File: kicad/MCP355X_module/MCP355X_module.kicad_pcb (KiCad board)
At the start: 2 copper layers, 20.8 x 15.7 mm, 20 parts, among them J1 PINS_1X6, J2 PINS_1X6, U1 MCP355X-E_SN

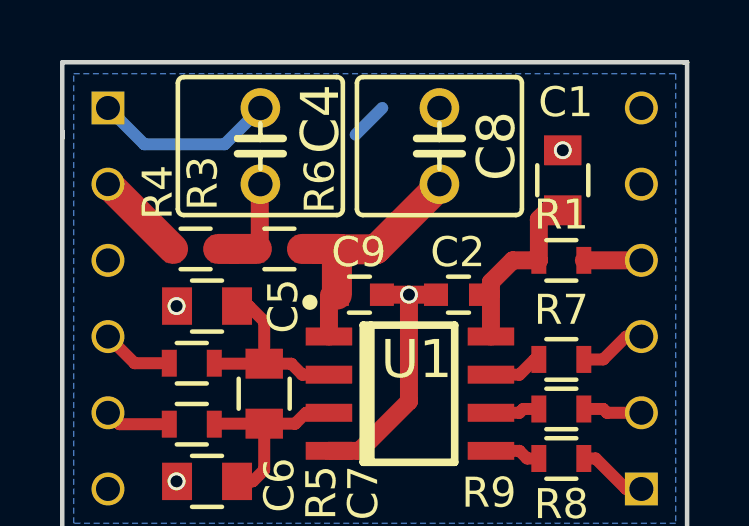
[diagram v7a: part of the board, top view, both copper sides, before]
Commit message: * changes a mistake on layouting on wrong grid
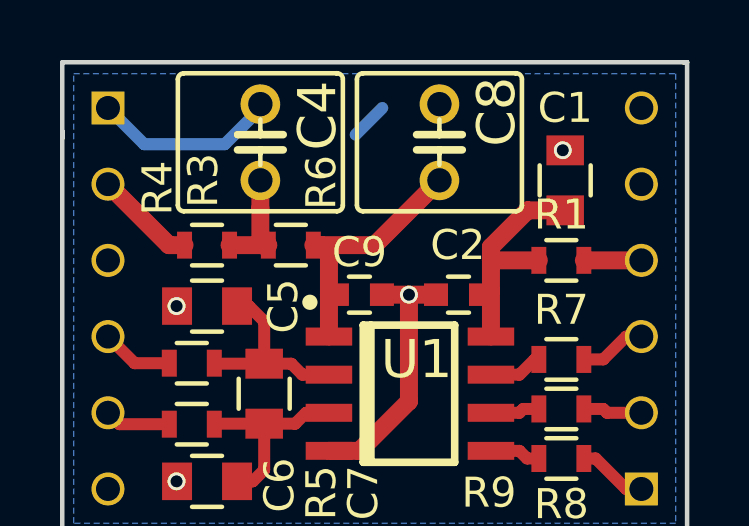
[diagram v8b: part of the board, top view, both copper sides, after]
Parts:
- moved R3 0.40 mm to (145.5, 102.4)
- moved R6 0.40 mm to (148.3, 102.4)
- moved C4 0.13 mm to (147.3, 98.9)
- moved C8 0.13 mm to (153.3, 98.9)
- moved C1 0.08 mm to (157.5, 100.2)
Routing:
- net VDD: track 6.34 -> 7.95 mm
- net GND: track 15.8 -> 14.5 mm
- net (no net): track 0.00 -> 1.26 mm
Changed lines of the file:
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@@
     (links 34)
     (no_connects 6)
-    (area 137.095 91.584714 165.375 115.21)
+    (area 137.095 91.571428 165.375 115.21)
     (thickness 1.6)
     (drawings 7)
-    (tracks 83)
+    (tracks 81)
     (zones 0)
     (modules 20)
@@
   )
   (setup
-    (last_trace_width 1)
+    (last_trace_width 0.6)
     (user_trace_width 0.3)
     (user_trace_width 0.4)
@@
     (tags "resistor 0603")
     (attr smd)
-    (fp_text reference R4 (at 1.134 5.699 450) (layer F.SilkS)
+    (fp_text reference R4 (at 1.143 5.842 450) (layer F.SilkS)
       (effects (font (size 1 1) (thickness 0.15)))
     )
@@
     (tags "capacitor 0603")
     (attr smd)
-    (fp_text reference C2 (at 0.024 1.413 360) (layer F.SilkS)
+    (fp_text reference C2 (at 0.024 1.651 360) (layer F.SilkS)
       (effects (font (size 1 1) (thickness 0.15)))
     )
@@
   )
   (module Resistors_SMD:R_0603 (layer F.Cu)
-    (at 145.161 102.489 180)
+    (at 145.542 102.362 180)
     (descr "Resistor SMD 0603, reflow soldering, Vishay (see dcrcw.pdf)")
     (tags "resistor 0603")
     (attr smd)
-    (fp_text reference R3 (at -0.239 2.189 270) (layer F.SilkS)
+    (fp_text reference R3 (at 0.127 2.159 270) (layer F.SilkS)
       (effects (font (size 1 1) (thickness 0.15)))
     )
@@
   )
   (module Resistors_SMD:R_0603 (layer F.Cu)
-    (at 147.955 102.489 180)
+    (at 148.336 102.362 180)
     (descr "Resistor SMD 0603, reflow soldering, Vishay (see dcrcw.pdf)")
     (tags "resistor 0603")
     (attr smd)
-    (fp_text reference R6 (at -1.345 2.089 270) (layer F.SilkS)
+    (fp_text reference R6 (at -1.016 2.089 270) (layer F.SilkS)
       (effects (font (size 1 1) (thickness 0.15)))
     )
@@
   )
   (module Capacitors_SMD:C_0805 (layer F.Cu)
-    (at 157.4 100.2 90)
+    (at 157.48 100.203 90)
     (descr "Capacitor SMD 0805, reflow soldering, AVX (see smccp.pdf)")
     (tags "capacitor 0805")
     (attr smd)
-    (fp_text reference C1 (at 2.6 0.1 360) (layer F.SilkS)
+    (fp_text reference C1 (at 2.413 0 360) (layer F.SilkS)
       (effects (font (size 1 1) (thickness 0.15)))
     )
@@
     (tags "capacitor 0603")
     (attr smd)
-    (fp_text reference C9 (at 0.022 1.413 180) (layer F.SilkS)
+    (fp_text reference C9 (at 0 1.413 180) (layer F.SilkS)
       (effects (font (size 1 1) (thickness 0.15)))
     )
@@
   )
   (module SquantorRcl:C025-055X046 (layer F.Cu)
-    (at 147.32 99.06 270)
+    (at 147.32 98.933 270)
     (descr CAPACITOR)
     (tags CAPACITOR)
     (attr virtual)
-    (fp_text reference C4 (at -0.9 -2 270) (layer F.SilkS)
+    (fp_text reference C4 (at -0.889 -1.905 270) (layer F.SilkS)
       (effects (font (size 1.27 1.27) (thickness 0.15)))
     )
@@
   )
   (module SquantorRcl:C025-055X046 (layer F.Cu)
-    (at 153.289 99.06 270)
+    (at 153.289 98.933 270)
     (descr CAPACITOR)
     (tags CAPACITOR)
     (attr virtual)
-    (fp_text reference C8 (at 0 -1.9 270) (layer F.SilkS)
+    (fp_text reference C8 (at -1.016 -1.905 270) (layer F.SilkS)
       (effects (font (size 1.27 1.27) (thickness 0.15)))
     )
@@
   (gr_line (start 161.544 112.014) (end 140.716 112.014) (angle 90) (layer Edge.Cuts) (width 0.15))
   (gr_line (start 140.716 96.266) (end 161.544 96.266) (angle 90) (layer Edge.Cuts) (width 0.15))
+  (segment (start 151.384 97.79) (end 150.495 98.679) (width 0.4) (layer B.Cu) (net 0))
   (segment (start 146.13 99) (end 143.45 99) (width 0.4) (layer B.Cu) (net 1))
   (segment (start 143.45 99) (end 142.24 97.79) (width 0.4) (layer B.Cu) (net 1))
@@
   (segment (start 144.526 104.394) (end 144.526 104.394) (width 0.6) (layer B.Cu) (net 1))
   (via (at 144.526 104.394) (size 0.6) (drill 0.4) (layers F.Cu B.Cu) (net 1))
-  (segment (start 151.384 97.79) (end 150.495 98.679) (width 0.4) (layer B.Cu) (net 1))
-  (segment (start 156.9 101.2) (end 156.603 101.497) (width 0.6) (layer F.Cu) (net 2))
-  (segment (start 156.603 101.497) (end 156.603 102.87) (width 0.6) (layer F.Cu) (net 2))
-  (segment (start 157.4 101.2) (end 156.9 101.2) (width 0.6) (layer F.Cu) (net 2))
-  (segment (start 155.006 103.594) (end 155.006 104) (width 0.6) (layer F.Cu) (net 2))
-  (segment (start 155.006 104) (end 155.006 105.41) (width 0.6) (layer F.Cu) (net 2))
-  (segment (start 154.674 104.013) (end 154.993 104.013) (width 0.6) (layer F.Cu) (net 2))
-  (segment (start 154.993 104.013) (end 155.006 104) (width 0.6) (layer F.Cu) (net 2))
-  (segment (start 155.73 102.87) (end 155.006 103.594) (width 0.6) (layer F.Cu) (net 2))
-  (segment (start 156.603 102.87) (end 155.73 102.87) (width 0.6) (layer F.Cu) (net 2))
+  (segment (start 155.006 105.41) (end 155.006 103.886) (width 0.6) (layer F.Cu) (net 2))
+  (segment (start 155.006 103.886) (end 155.006 102.87) (width 0.6) (layer F.Cu) (net 2))
+  (segment (start 154.674 104.013) (end 154.879 104.013) (width 0.6) (layer F.Cu) (net 2))
+  (segment (start 154.879 104.013) (end 155.006 103.886) (width 0.6) (layer F.Cu) (net 2))
+  (segment (start 155.006 102.87) (end 155.006 102.423) (width 0.6) (layer F.Cu) (net 2))
+  (segment (start 156.603 102.87) (end 155.006 102.87) (width 0.6) (layer F.Cu) (net 2))
+  (segment (start 155.006 102.423) (end 156.226 101.203) (width 0.6) (layer F.Cu) (net 2))
+  (segment (start 156.226 101.203) (end 157.48 101.203) (width 0.6) (layer F.Cu) (net 2))
   (segment (start 160.02 105.41) (end 159.512 105.41) (width 0.4) (layer F.Cu) (net 3))
   (segment (start 159.512 105.41) (end 158.75 106.172) (width 0.4) (layer F.Cu) (net 3))
@@
   (segment (start 158.75 107.823) (end 158.103 107.823) (width 0.4) (layer F.Cu) (net 9))
   (segment (start 158.877 107.95) (end 158.75 107.823) (width 0.4) (layer F.Cu) (net 9))
+  (segment (start 142.24 100.33) (end 144.272 102.362) (width 0.6) (layer F.Cu) (net 10))
+  (segment (start 144.272 102.362) (end 144.792 102.362) (width 0.6) (layer F.Cu) (net 10))
   (segment (start 142.24 100.33) (end 142.252 100.33) (width 1) (layer F.Cu) (net 10))
-  (segment (start 142.252 100.33) (end 144.411 102.489) (width 1) (layer F.Cu) (net 10))
-  (segment (start 147.3 100.37) (end 147.3 102.394) (width 0.6) (layer F.Cu) (net 11))
-  (segment (start 147.3 102.394) (end 147.205 102.489) (width 0.6) (layer F.Cu) (net 11))
-  (segment (start 145.911 102.489) (end 146.431 102.489) (width 1) (layer F.Cu) (net 11))
-  (segment (start 146.431 102.489) (end 147.205 102.489) (width 1) (layer F.Cu) (net 11))
+  (segment (start 146.292 102.362) (end 147.32 102.362) (width 0.6) (layer F.Cu) (net 11))
+  (segment (start 147.32 102.362) (end 147.586 102.362) (width 0.6) (layer F.Cu) (net 11))
+  (segment (start 147.32 100.203) (end 147.32 101.136946) (width 0.6) (layer F.Cu) (net 11))
+  (segment (start 147.32 101.136946) (end 147.32 102.362) (width 0.6) (layer F.Cu) (net 11))
   (segment (start 146.542 104.394) (end 146.939 104.394) (width 0.4) (layer F.Cu) (net 12))
   (segment (start 146.939 104.394) (end 147.447 104.902) (width 0.4) (layer F.Cu) (net 12))
@@
   (segment (start 148.844 107.95) (end 148.479 108.315) (width 0.4) (layer F.Cu) (net 13))
   (segment (start 148.479 108.315) (end 147.447 108.315) (width 0.4) (layer F.Cu) (net 13))
-  (segment (start 148.705 102.489) (end 149.2 102.489) (width 1) (layer F.Cu) (net 14))
-  (segment (start 149.872 104.013) (end 149.872 102.638) (width 1) (layer F.Cu) (net 14))
-  (segment (start 149.723 102.489) (end 149.2 102.489) (width 1) (layer F.Cu) (net 14))
-  (segment (start 149.2 102.489) (end 149.955 102.489) (width 1) (layer F.Cu) (net 14))
-  (segment (start 149.872 102.638) (end 149.723 102.489) (width 1) (layer F.Cu) (net 14))
-  (segment (start 149.966 102.5) (end 151.17 102.5) (width 1) (layer F.Cu) (net 14))
-  (segment (start 151.17 102.5) (end 153.3 100.37) (width 1) (layer F.Cu) (net 14))
-  (segment (start 149.955 102.489) (end 149.966 102.5) (width 1) (layer F.Cu) (net 14))
-  (segment (start 149.606 105.41) (end 149.606 104.013) (width 0.6) (layer F.Cu) (net 14))
+  (segment (start 153.289 100.203) (end 151.13 102.362) (width 0.6) (layer F.Cu) (net 14))
+  (segment (start 151.13 102.362) (end 149.352 102.362) (width 0.6) (layer F.Cu) (net 14))
+  (segment (start 149.606 102.616) (end 149.606 104.013) (width 0.6) (layer F.Cu) (net 14))
+  (segment (start 149.606 104.013) (end 149.606 105.41) (width 0.6) (layer F.Cu) (net 14))
+  (segment (start 149.872 104.013) (end 149.606 104.013) (width 0.6) (layer F.Cu) (net 14))
+  (segment (start 149.352 102.362) (end 149.606 102.616) (width 0.6) (layer F.Cu) (net 14))
+  (segment (start 149.086 102.362) (end 149.352 102.362) (width 0.6) (layer F.Cu) (net 14))
   (segment (start 144.284 106.299) (end 143.129 106.299) (width 0.4) (layer F.Cu) (net 15))
   (segment (start 143.129 106.299) (end 142.24 105.41) (width 0.4) (layer F.Cu) (net 15))
@@
     (polygon
       (pts
-        (xy 142.494 101.219) (xy 144.272 102.997) (xy 153.67 102.997) (xy 153.67 101.727) (xy 144.272 101.727)
+        (xy 142.494 101.219) (xy 144.272 102.997) (xy 150.622 102.997) (xy 150.622 101.727) (xy 144.272 101.727)
         (xy 143.129 100.584)
       )
